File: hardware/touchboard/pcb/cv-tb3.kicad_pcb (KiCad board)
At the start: 2 copper layers, 88.5 x 117 mm, 62 parts, among them J1 2P 5.08mm, J2 3P 5.08mm, J3 3P 5.08mm, J4 3P 2.54mm, K1 SRD-05VDC-SL-C, K2 SRD-05VDC-SL-C, K3 SRD-05VDC-SL-C, Q1 S8050, Q2 S8050, Q3 S8050, Q4 S8050, SW1 6mm tactile, U1 ESP32-WROOM-32E (4MB), U2 AMS1117-3.3, U3 PC817, U4 PC817, U5 PC817, U6 BL0937 / HLW8012

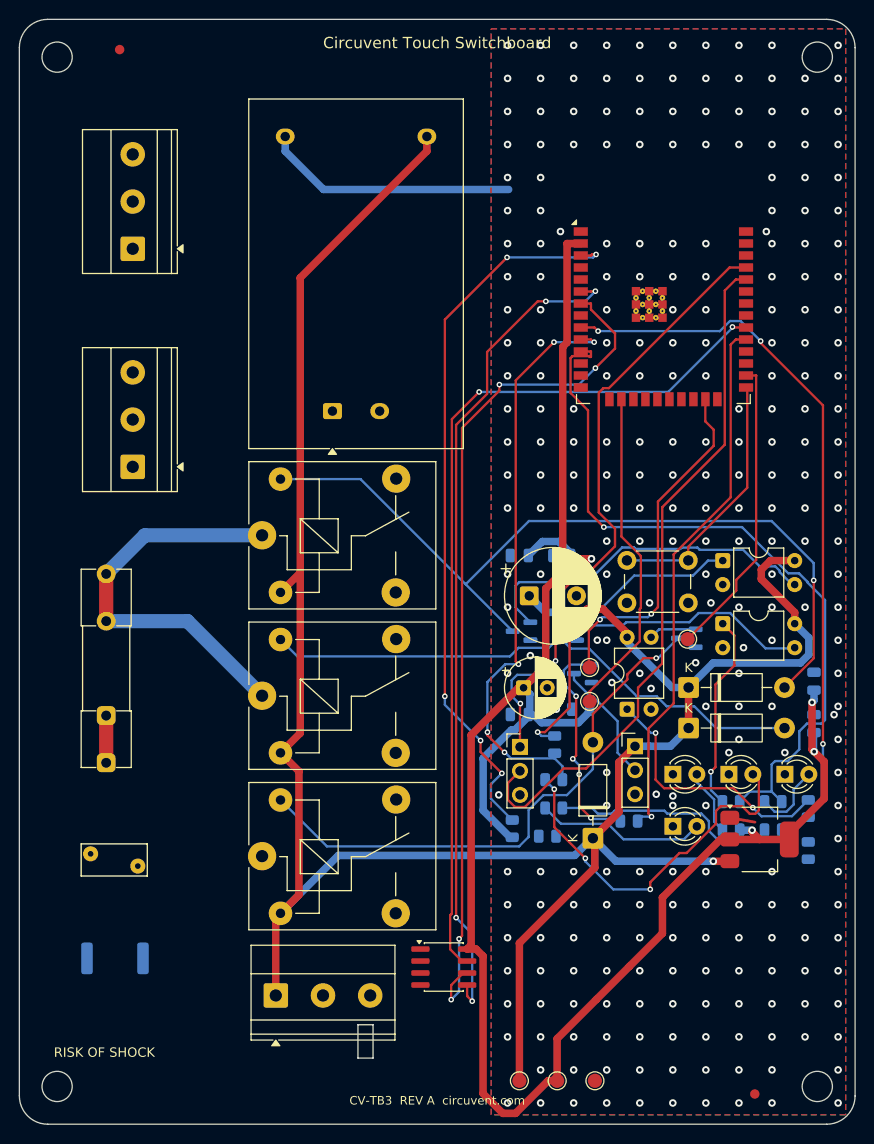
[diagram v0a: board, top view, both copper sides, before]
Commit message: hardware: in-house 230VAC to 5V/3V3 isolated flyback to replace the HLK module
Twelve boards buy a Hi-Link HLK-PM03 and then spend an AMS1117 getting 3.3 V
out of it. This adds psu-5v3v3: a TNY274 flyback with opto/TL431 feedback that
produces both rails, so the host board drops its LDO and we stop depending on
one vendor for the part that makes everything else work.

New in the generator:

- hardware/lib/Circuvent.pretty, a repo-local footprint library, because KiCad
  ships no flyback bobbin and no safety-capacitor land. load_fp() prefers it
  over the KiCad install so a clean checkout rebuilds. The footprints are
  generated by make_lib.py, where every dimension is a named constant - the
  EE13 bobbin is a de facto standard rather than a controlled one, so that
  file is where you reconcile it with whoever winds the transformer.
- build_netlist_psu(), because a PSU has no MCU and the existing builder is
  organised around one.
- An HVDC netclass. Marking the whole primary as MAINS is correct about the
  hazard and wrong about the current: it forced 1.5 mm track and 2.0 mm
  clearance onto the BYPASS decoupling, and 33 of 33 primary nets failed to
  route. HVDC keeps a mains-grade gap to SELV and a sane one to itself.
- That split then broke reinforced_mains_to_selv, which excluded only MAINS
  and so began demanding 8 mm between AC_N and HV+ - two nets on the same side
  of the barrier, inside the same island. The two hazardous classes are now
  exempt from each other and both 8 mm from everything else.

Review found three defects in my own RCD clamp before it was committed: the
catch diode returned to the rail instead of catching at the drain, leaving the
leakage spike nowhere to go; the two snubber resistors were wired in parallel,
which halves the resistance instead of sharing the 325 V; and a decoupling cap
was orphaned.

The board is NOT fabricable as generated and the file says so. Thirteen
clearance errors remain, all primary copper against the optocoupler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
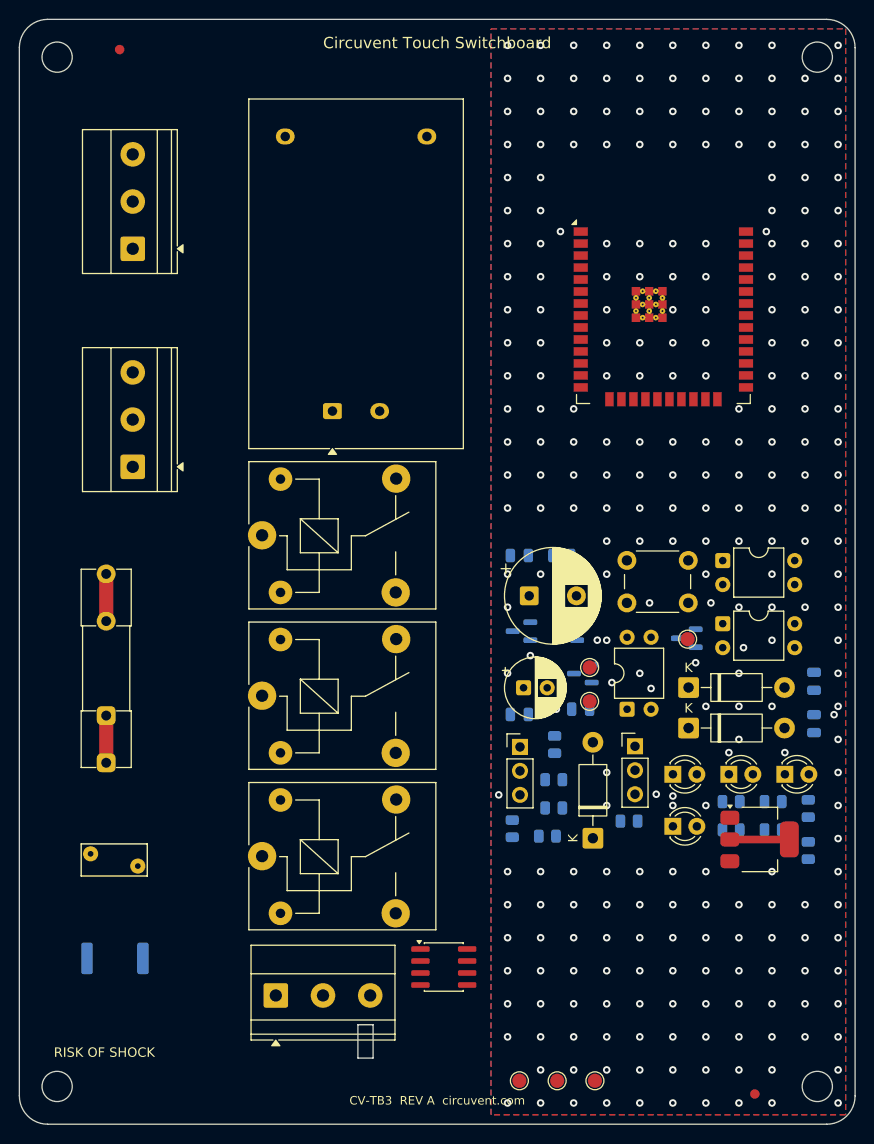
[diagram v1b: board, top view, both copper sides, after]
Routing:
- net +5V: track 256.4 -> 0.00 mm, vias 2 -> 0
- net +3V3: track 209.0 -> 6.30 mm, vias 4 -> 0
- net RELAY3: track 103.8 -> 0.00 mm, vias 3 -> 0
- net MTR_SEL: track 93.8 -> 0.00 mm, vias 2 -> 0
- net MTR_CF1: track 91.7 -> 0.00 mm, vias 4 -> 0
- net MTR_CF: track 88.4 -> 0.00 mm, vias 4 -> 0
- net RELAY1_COIL: track 87.2 -> 0.00 mm, vias 1 -> 0
- net RELAY2: track 79.6 -> 0.00 mm, vias 1 -> 0
- net EN: track 77.4 -> 0.00 mm, vias 5 -> 0
- net UART_RX: track 73.3 -> 0.00 mm
- net UART_TX: track 66.3 -> 0.00 mm, vias 2 -> 0
- net RELAY1: track 62.7 -> 0.00 mm, vias 5 -> 0
- net RELAY2_COIL: track 59.6 -> 0.00 mm
- net RELAY3_COIL: track 58.6 -> 0.00 mm, vias 1 -> 0
- net BACKLIGHT: track 57.2 -> 0.00 mm, vias 1 -> 0
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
